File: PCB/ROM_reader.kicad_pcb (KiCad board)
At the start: 2 copper layers, 94 x 59 mm, 47 parts, among them J1 USB_B_Mini, J2 TTL_UART, J3 ISP, J4 RAM ADAPTER EXT, J5 ROM MODULE, SW1 RST, U1 CH340G, U2 ATmega128A-A, Y1 12MHz, Y2 7.3728MHz

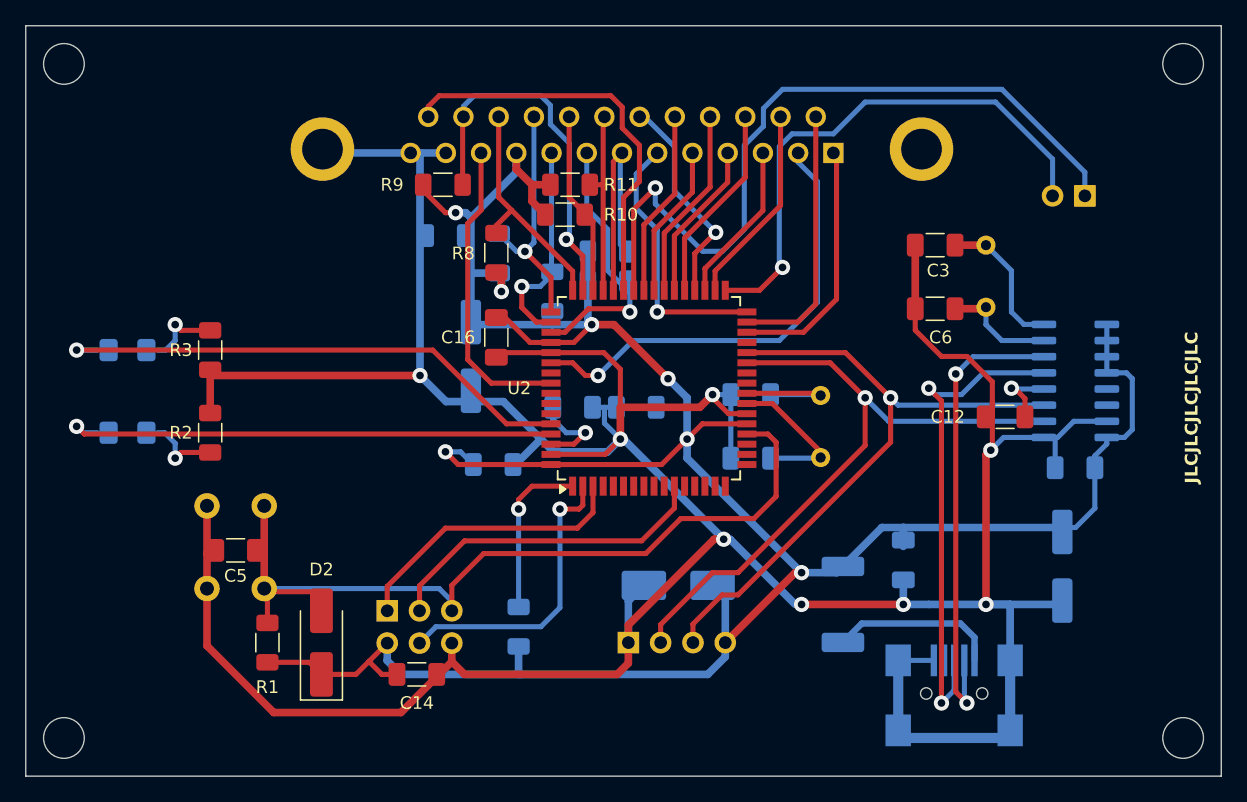
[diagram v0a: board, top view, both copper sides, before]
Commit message: miniUSB socket replaced with USB C socket. PCB now at revision D
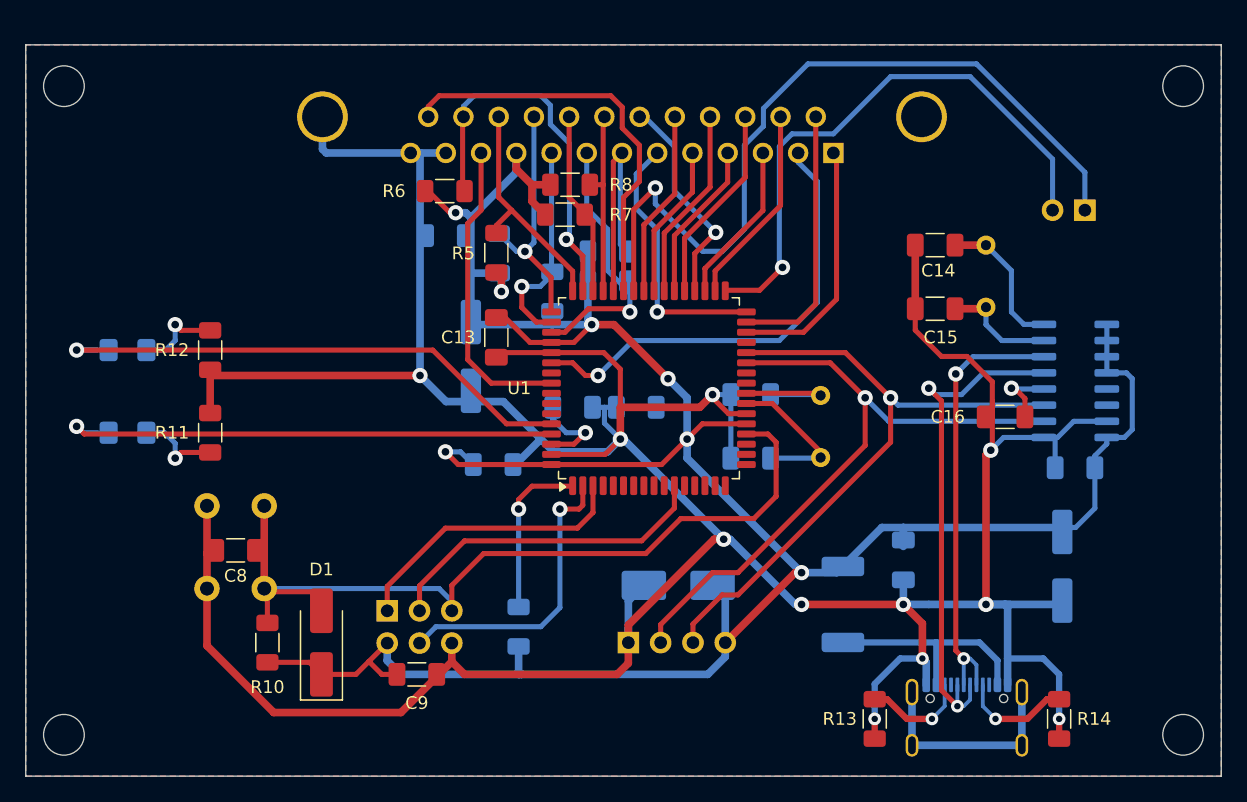
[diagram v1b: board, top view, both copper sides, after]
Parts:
- removed the J1 at (165.0, 113.0)
- added J5: USB C SOCKET, Connector_USB:USB_C_Receptacle_GCT_USB4105-xx-A_16P_TopMnt_Horizontal, B.Cu at (166.0, 116.0)
- added R13: 5k1, Resistor_SMD:R_1206_3216Metric_Pad1.30x1.75mm_HandSolder, F.Cu at (158.8, 115.0)
- added R14: 5k1, Resistor_SMD:R_1206_3216Metric_Pad1.30x1.75mm_HandSolder, F.Cu at (173.2, 115.0)
- J1: renamed from J5; footprint Connector_Dsub:DSUB-25_Female_Horizontal_P2.77x2.84mm_EdgePinOffset4.94mm_Housed_MountingHolesOffset7.48mm -> Connector_Dsub:DSUB-25_Socket_Horizontal_P2.77x2.84mm_EdgePinOffset4.94mm_Housed_MountingHolesOffset4.94mm
- moved H1 1.75 mm to (95.0, 65.2)
- moved H3 1.75 mm to (183.0, 65.2)
- moved J2 1.12 mm to (175.3, 75.0)
- moved R6 0.52 mm to (125.0, 73.5)
- moved H2 0.25 mm to (183.0, 116.2)
- moved H4 0.25 mm to (95.0, 116.2)
- renumbered C15 to C10, C8 to C11, C13 to C12, C16 to C13, C3 to C14, C6 to C15, C12 to C16, C4 to C3, C7 to C4, C9 to C5, C10 to C6, C11 to C7, C5 to C8, C14 to C9, D2 to D1, D1 to D2, J4 to J2, J2 to J4, R4 to R1, R1 to R10, R2 to R11, R3 to R12, R5 to R2, R6 to R3, R7 to R4, R8 to R5, R9 to R6, R10 to R7, R11 to R8, R12 to R9, U2 to U1, U1 to U2, Y2 to Y1, Y1 to Y2
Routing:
- net GND: track 301.1 -> 325.1 mm, vias 8 -> 11
- net Net-(J5-CC1): track 0.00 -> 8.24 mm, vias 0 -> 1
- net Net-(J5-CC2): track 0.00 -> 7.74 mm, vias 0 -> 1
- net Net-(F1-Pad1): track 13.2 -> 18.0 mm
- net A15_RAM_ADAPTER: track 59.8 -> 62.6 mm
- net #WR: track 42.5 -> 45.3 mm
- net Net-(U2-UD-): track 37.2 -> 35.0 mm
- net Net-(U2-UD+): track 38.9 -> 40.0 mm
- net /D4: track 29.5 -> 30.3 mm
- net +5V: track 220.2 -> 219.6 mm
- added copper zone on B.Cu, net GND
- added copper zone on F.Cu, net GND
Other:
- board size 94 x 59 mm -> 94 x 57.5 mm
- board text removed: "JLCJLCJLCJLCJLC"
